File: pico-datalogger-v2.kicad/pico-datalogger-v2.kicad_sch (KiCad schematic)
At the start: 41 parts, among them J1 JST-PH2 Bat, J10 Conn_PCB_2, J11 Conn_I2C1, J12 Conn_UART_5V, J13 Conn_I2C1, J14 Conn_I2C0, J15 PCB_2_THT, J16 LoRa_THT, J17 Disp_THT, J2 Conn_Pico_Left, J3 Conn_Pico_Right, J4 PCB_1_THT, J5 Conn_LoRa, J6 Conn_Display, J7 Conn_PCB_1, J8 Conn_ADC, J9 Conn_I2C0, Q1 AO3401A, Q2 AO3401A, SW1 SW_ON, SW2 SW_RST, U1 74LVC2G74, U2 PCF8523T, U3 Pico, U4 XTSD, Y1 Crystal

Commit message: Datalogger-v2 Rev 2.00: larger PCB-size, THT-connectors (ready for prod)
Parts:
- SW1, SW2: now left out of the parts list
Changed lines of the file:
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@@
   (title_block
     (title "pico-datalogger-v2")
-    (date "2024-01-25")
-    (rev "1.95")
+    (date "2024-01-26")
+    (rev "2.00")
     (company "Bernhard Bablok")
     (comment 1 "https://github.com/bablokb/pcb-pico-datalogger")
@@
   )
   (symbol (lib_id "user:SW_Push_Vertical") (at 100.076 186.436 0) (unit 1)
-    (in_bom yes) (on_board yes)
+    (in_bom no) (on_board yes)
     (property "Reference" "SW2" (id 0) (at 100.33 178.816 0))
     (property "Value" "SW_RST" (id 1) (at 100.076 181.61 0))
@@
   )
   (symbol (lib_name "SW_Push_Vertical_1") (lib_id "user:SW_Push_Vertical") (at 220.726 68.58 0) (unit 1)
-    (in_bom yes) (on_board yes)
+    (in_bom no) (on_board yes)
     (property "Reference" "SW1" (id 0) (at 220.98 60.96 0))
     (property "Value" "SW_ON" (id 1) (at 220.726 63.754 0))

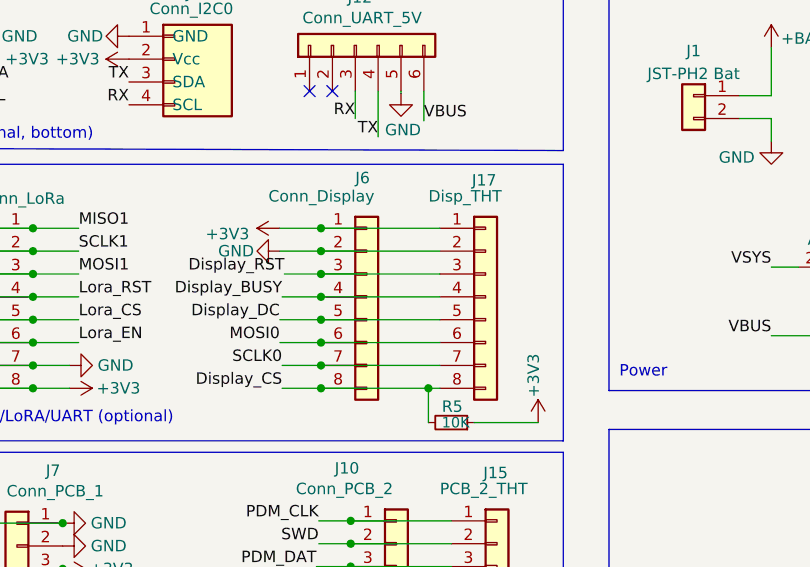
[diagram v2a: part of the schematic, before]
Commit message: Datalogger-v2 Rev 2.01: rotated display connector (ready for prod)
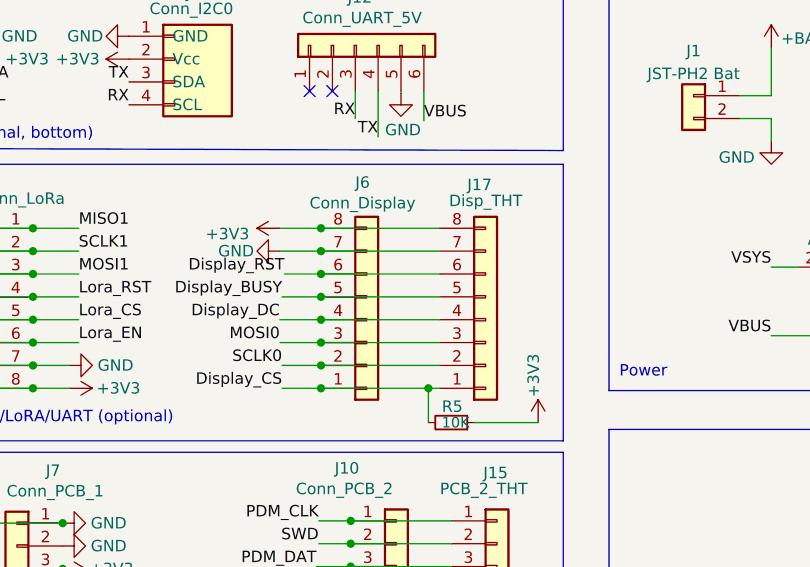
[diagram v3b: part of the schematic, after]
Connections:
- net +3V3: now also J17.8 (Pin_8), J6.8 (Pin_8); no longer J17.1 (Pin_1), J6.1 (Pin_1)
- net Display_BUSY: now also J17.5 (Pin_5), J6.5 (Pin_5); no longer J17.4 (Pin_4), J6.4 (Pin_4)
- net Display_CS: now also J17.1 (Pin_1), J6.1 (Pin_1); no longer J17.8 (Pin_8), J6.8 (Pin_8)
- net Display_DC: now also J17.4 (Pin_4), J6.4 (Pin_4); no longer J17.5 (Pin_5), J6.5 (Pin_5)
- net Display_RST: now also J17.6 (Pin_6), J6.6 (Pin_6); no longer J17.3 (Pin_3), J6.3 (Pin_3)
- net GND: now also J17.7 (Pin_7), J6.7 (Pin_7); no longer J17.2 (Pin_2), J6.2 (Pin_2)
- net MOSI0: now also J17.3 (Pin_3), J6.3 (Pin_3); no longer J17.6 (Pin_6), J6.6 (Pin_6)
- net SCLK0: now also J17.2 (Pin_2), J6.2 (Pin_2); no longer J17.7 (Pin_7), J6.7 (Pin_7)
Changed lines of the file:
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@@
   (title_block
     (title "pico-datalogger-v2")
-    (date "2024-01-26")
-    (rev "2.00")
+    (date "2024-02-01")
+    (rev "2.01")
     (company "Bernhard Bablok")
     (comment 1 "https://github.com/bablokb/pcb-pico-datalogger")
@@
     (pin "1")
   )
-  (symbol (lib_id "Connector_Generic:Conn_01x08") (at 173.736 116.332 0) (unit 1)
+  (symbol (lib_id "Connector_Generic:Conn_01x08") (at 173.736 118.872 0) (mirror x) (unit 1)
     (in_bom yes) (on_board yes)
-    (property "Reference" "J6" (id 0) (at 172.466 103.124 0)
+    (property "Reference" "J6" (id 0) (at 172.466 103.632 0)
       (effects (font (size 1.27 1.27)) (justify left))
     )
-    (property "Value" "Conn_Display" (id 1) (at 162.814 105.156 0)
+    (property "Value" "Conn_Display" (id 1) (at 167.386 105.918 0)
       (effects (font (size 1.27 1.27)) (justify left))
     )
-    (property "Footprint" "Connector_JST:JST_SUR_BM08B-SURS-TF_1x08-1MP_P0.80mm_Vertical" (id 2) (at 173.736 116.332 0)
-      (effects (font (size 1.27 1.27)) hide)
-    )
-    (property "Datasheet" "~" (id 3) (at 173.736 116.332 0)
-      (effects (font (size 1.27 1.27)) hide)
-    )
-    (property "LCSC" "C5143489" (id 4) (at 173.736 116.332 0)
+    (property "Footprint" "Connector_JST:JST_SUR_BM08B-SURS-TF_1x08-1MP_P0.80mm_Vertical" (id 2) (at 173.736 118.872 0)
+      (effects (font (size 1.27 1.27)) hide)
+    )
+    (property "Datasheet" "~" (id 3) (at 173.736 118.872 0)
+      (effects (font (size 1.27 1.27)) hide)
+    )
+    (property "LCSC" "C5143489" (id 4) (at 173.736 118.872 0)
       (effects (font (size 1.27 1.27)) hide)
     )
@@
     (pin "1")
   )
-  (symbol (lib_id "Connector_Generic:Conn_01x08") (at 186.944 116.332 0) (unit 1)
+  (symbol (lib_id "Connector_Generic:Conn_01x08") (at 186.944 118.872 0) (mirror x) (unit 1)
     (in_bom no) (on_board yes)
-    (property "Reference" "J17" (id 0) (at 185.42 103.378 0)
+    (property "Reference" "J17" (id 0) (at 184.912 103.886 0)
       (effects (font (size 1.27 1.27)) (justify left))
     )
-    (property "Value" "Disp_THT" (id 1) (at 180.594 105.156 0)
+    (property "Value" "Disp_THT" (id 1) (at 182.88 105.664 0)
       (effects (font (size 1.27 1.27)) (justify left))
     )
-    (property "Footprint" "Connector_PinHeader_2.54mm:PinHeader_1x08_P2.54mm_Vertical" (id 2) (at 186.944 116.332 0)
-      (effects (font (size 1.27 1.27)) hide)
-    )
-    (property "Datasheet" "~" (id 3) (at 186.944 116.332 0)
-      (effects (font (size 1.27 1.27)) hide)
-    )
+    (property "Footprint" "Connector_PinHeader_2.54mm:PinHeader_1x08_P2.54mm_Vertical" (id 2) (at 186.944 118.872 0)
+      (effects (font (size 1.27 1.27)) hide)
+    )
+    (property "Datasheet" "~" (id 3) (at 186.944 118.872 0)
+      (effects (font (size 1.27 1.27)) hide)
+    )

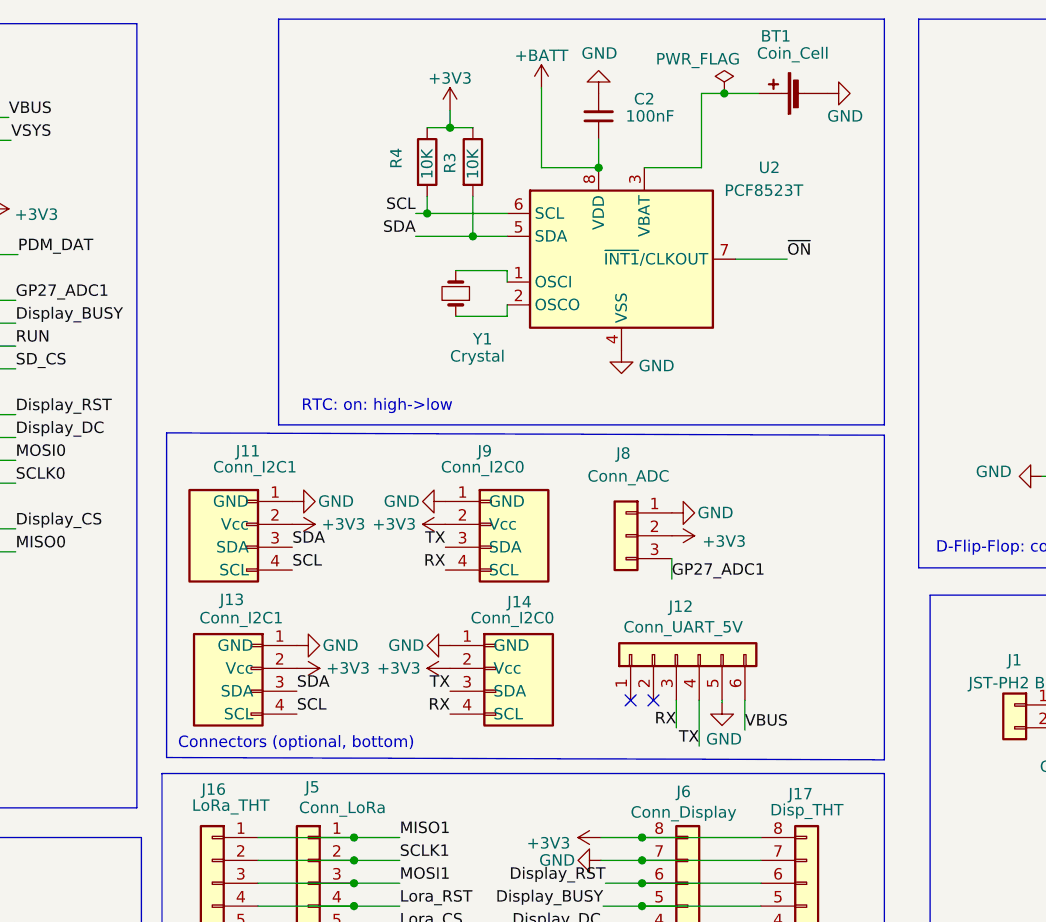
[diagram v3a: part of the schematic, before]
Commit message: Datalogger-v2 Rev 2.10: Stemma/Qt on top (ready for prod)
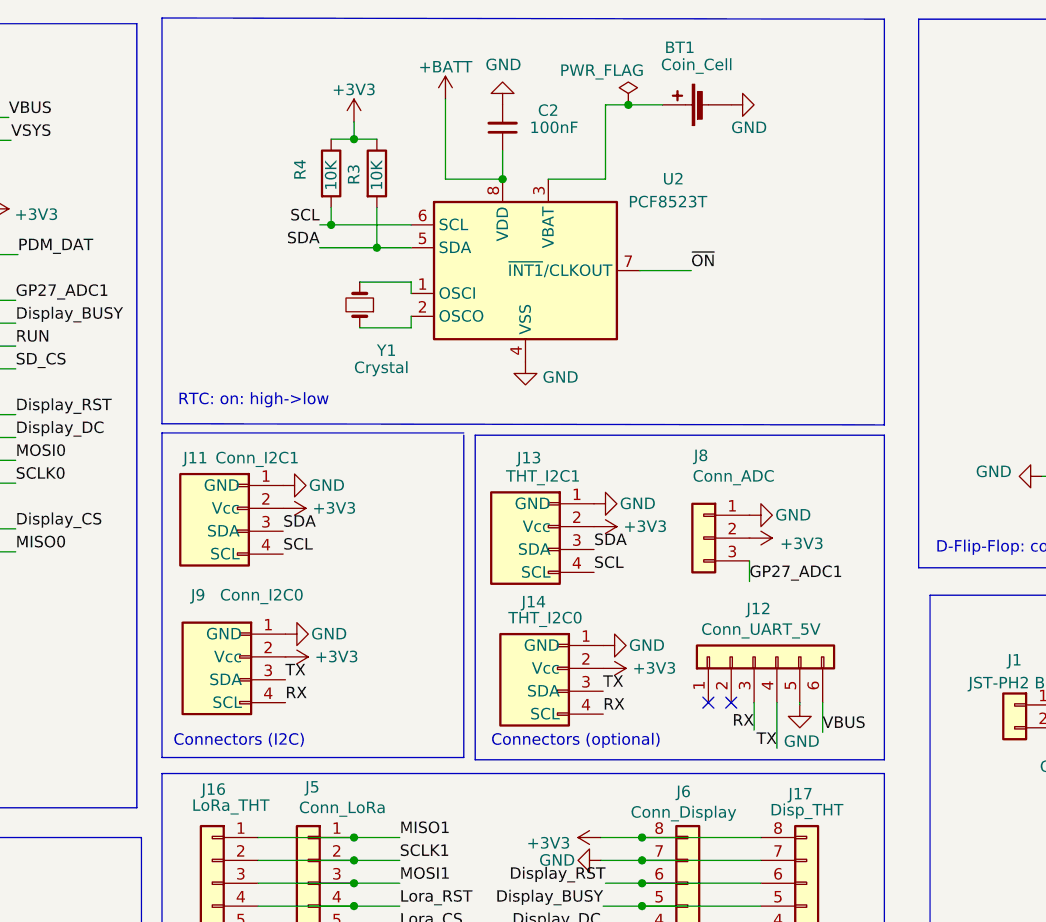
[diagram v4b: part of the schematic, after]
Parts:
- J11, J9: LCSC (none) -> C160404; now in the parts list
- J13: value Conn_I2C1 -> THT_I2C1
- J14: value Conn_I2C0 -> THT_I2C0
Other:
- note added: "Connectors (I2C)"
- note added: "Connectors (optional)"
- note removed: "Connectors (optional, bottom)"
- moved on the sheet: BT1, C2, J11, J12, J13, J14, J8, J9, R3, R4, U2, Y1
